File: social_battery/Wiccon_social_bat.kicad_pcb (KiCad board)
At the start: 2 copper layers, 84.5 x 43.3 mm, 20 parts, among them J1 SAO, SW1 Change, U1 CH32V003

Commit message: Change LCSC number of 100n capacitor on social battery
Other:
- board text added: "WICCA is a circle of women in cybersecurity based in The Netherlands with a vision to spread the cybersecurity word to everyone. WomenOfWicca.nl"

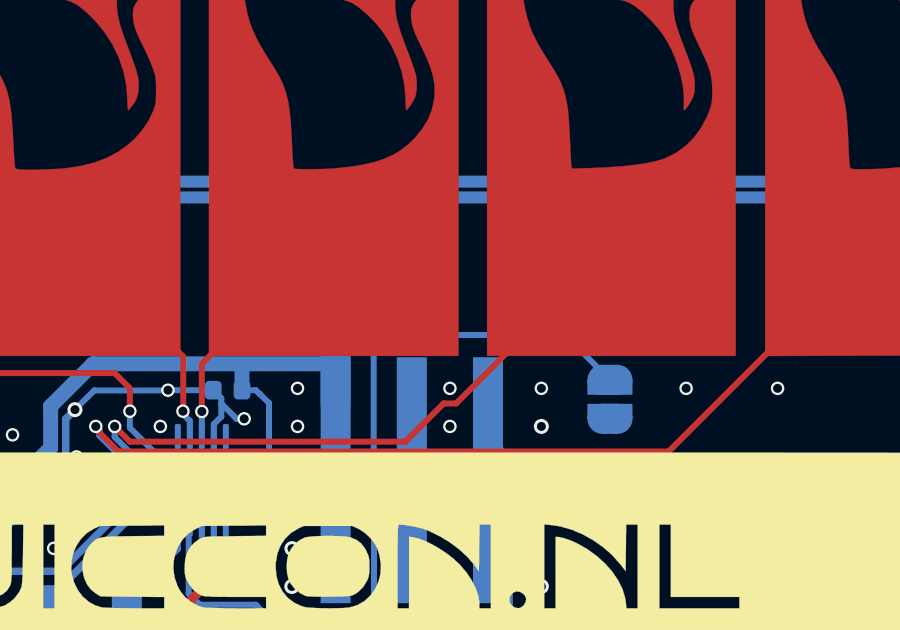
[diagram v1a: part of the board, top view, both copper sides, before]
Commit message: Add 100k pull-up to SDA on social battery and use correct footprint for battery holder on SAO nametag
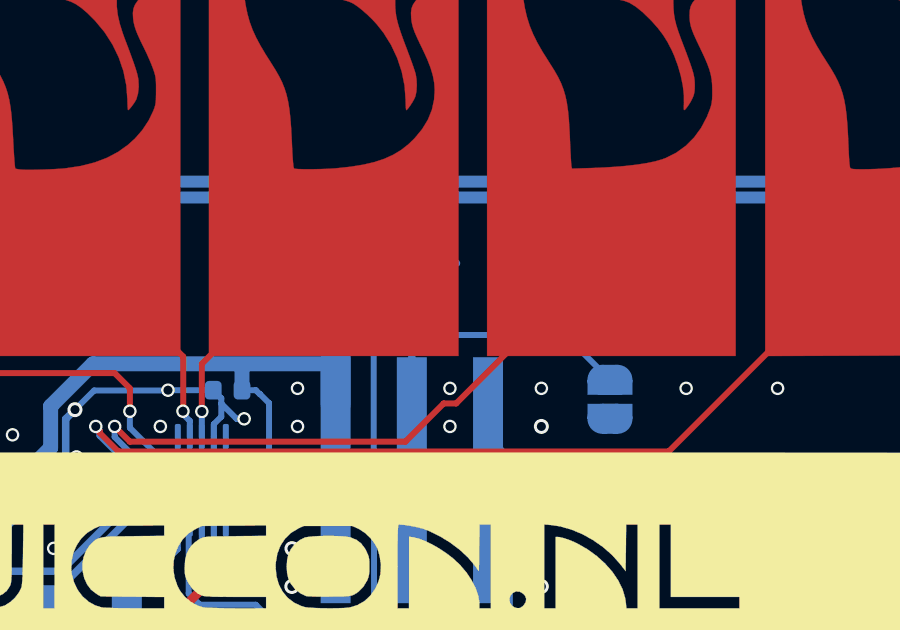
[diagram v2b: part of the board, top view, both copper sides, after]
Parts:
- added R2: 100k, Resistor_SMD:R_0402_1005Metric, B.Cu at (-0.51, 8.56)
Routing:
- net +3.3V: track 77.4 -> 82.0 mm
- net SDA: track 6.07 -> 9.98 mm
- net GND: track 17.7 -> 21.3 mm
- net Net-(JP1-B): track 16.8 -> 20.4 mm
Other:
- board text added: "Nicolai Electronics"
